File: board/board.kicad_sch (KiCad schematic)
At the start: 5 parts, among them J1 003_power, J2 003_power

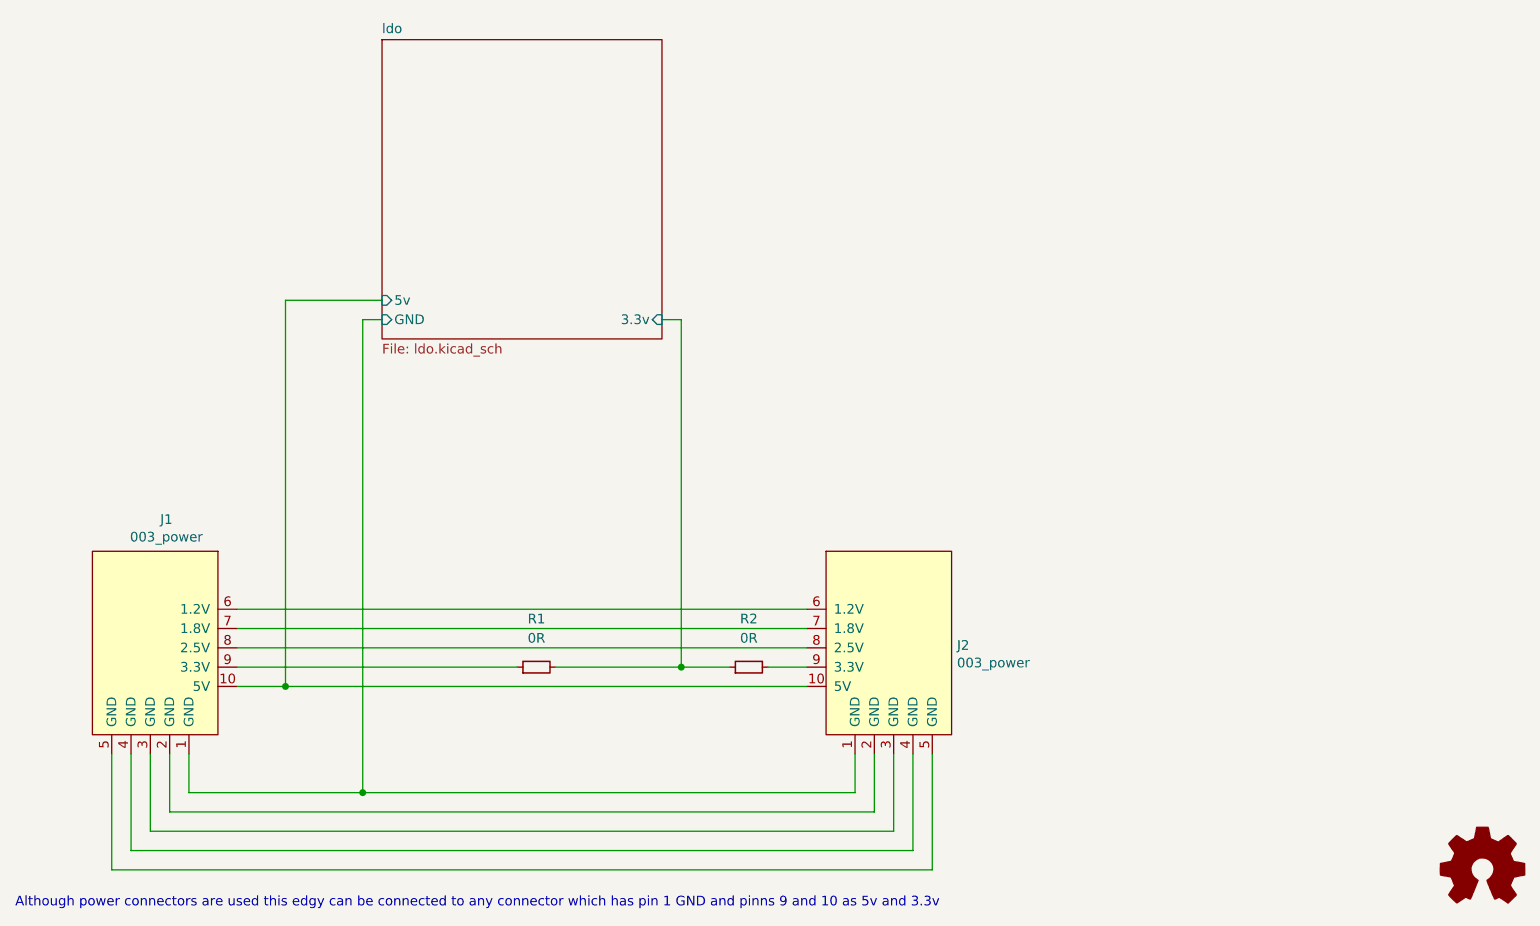
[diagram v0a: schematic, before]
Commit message: modernized layout to use 000 generic power symbols. the layout and thereofore the hardware version number is unaffected
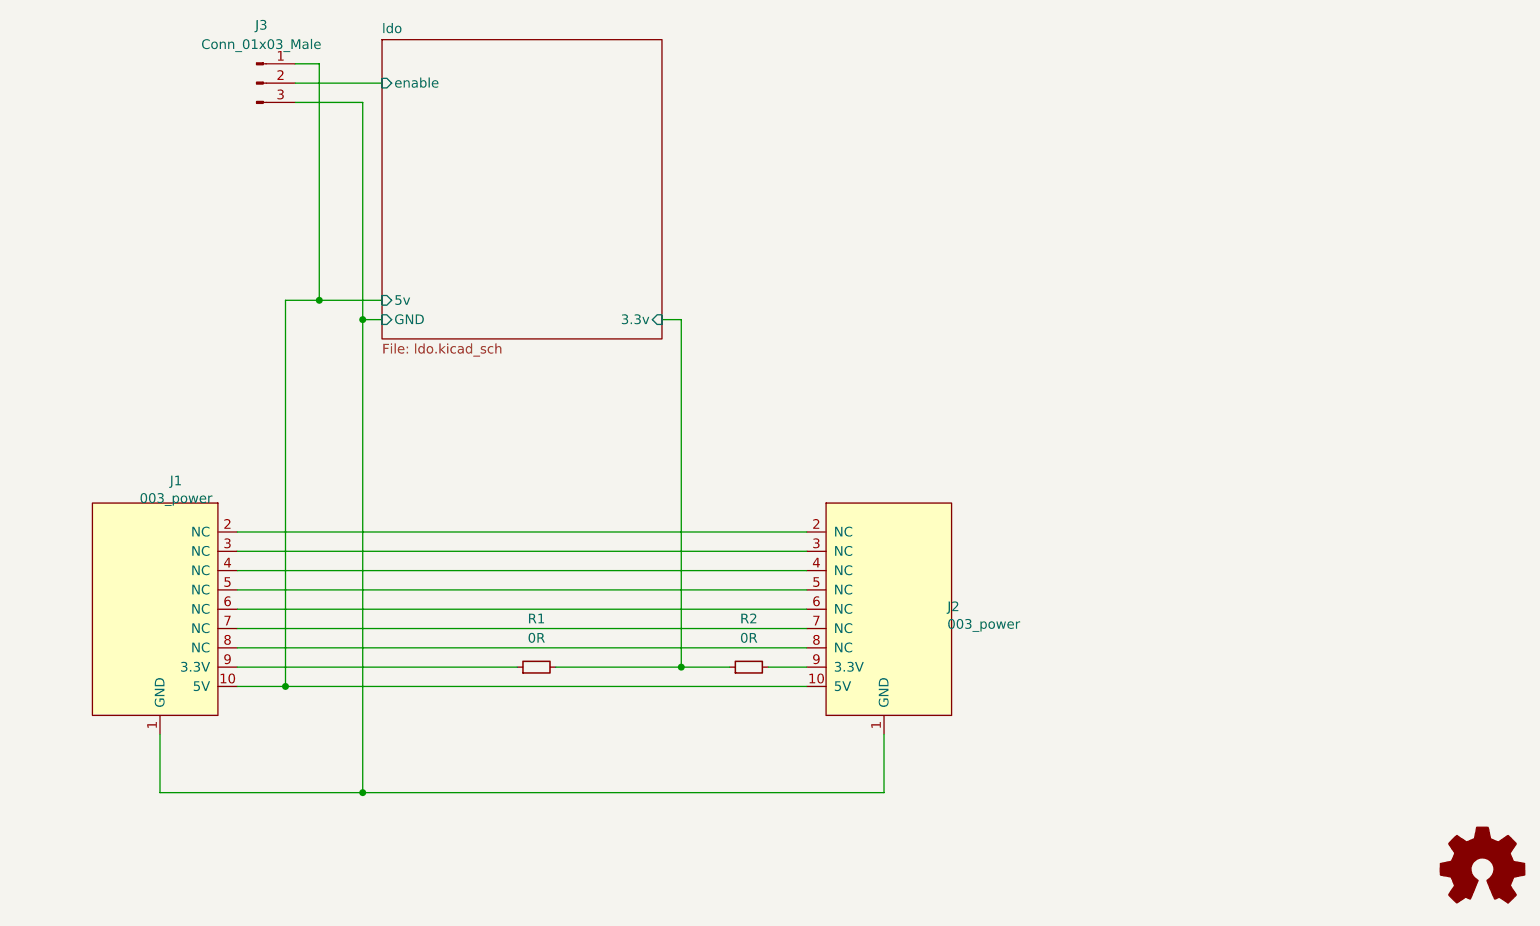
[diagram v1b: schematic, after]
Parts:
- added J3: Conn_01x03_Male, Connector_PinHeader_2.54mm:PinHeader_1x03_P2.54mm_Vertical, symbol Connector:Conn_01x03_Male
- J1, J2: symbol put_on_edge:003_power -> put_on_edge:000_3.3v_5v
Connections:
- net ldo/5v: now also J3.1 (Pin_1)
- net ldo/GND: now also J3.3 (Pin_3)
- new net ldo/enable: J3.2 (Pin_2)
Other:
- sheet ldo ports: added enable; removed none
- note removed: "Although power connectors are used this edgy can be connected to any connector which has pin 1 GND and pinns 9 and 10 as 5v and 3.3v"
- moved on the sheet: J1, J2
